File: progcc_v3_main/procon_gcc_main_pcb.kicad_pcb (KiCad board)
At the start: 4 copper layers, 110.9 x 59.7 mm, 108 parts, among them J1 Rumble, J2 Rumble, J3 To Button Board, J4 Conn_01x06_Female, J5 Conn_01x02_Pin, J9 USB_C_Receptacle, P1 Endpoint, Q1 Q_PMOS_GDS, Q2 Q_NMOS_GSD, Q3 Q_NMOS_GSD, Q4 BSS138, Q5 BSS138, Q6 BSS138, SW1 GL18_SW, SW2 GL18_SW, SW3 TS-1187A-B-A-B, T1 36-8730, T2 36-8730, T3 36-8730, T4 36-8730, U1 GH39F (Hall SOT23), U10 MCP3002, U11 ST_LSM6, U2 GH39F (Hall SOT23), U3 GH39F (Hall SOT23), U4 GH39F (Hall SOT23), U5 ST_LSM6, U6 RP2040, U7 LP3986-33B3F, U8 MCP3002, U9 W25Q128JVS, Y1 Crystal_GND3

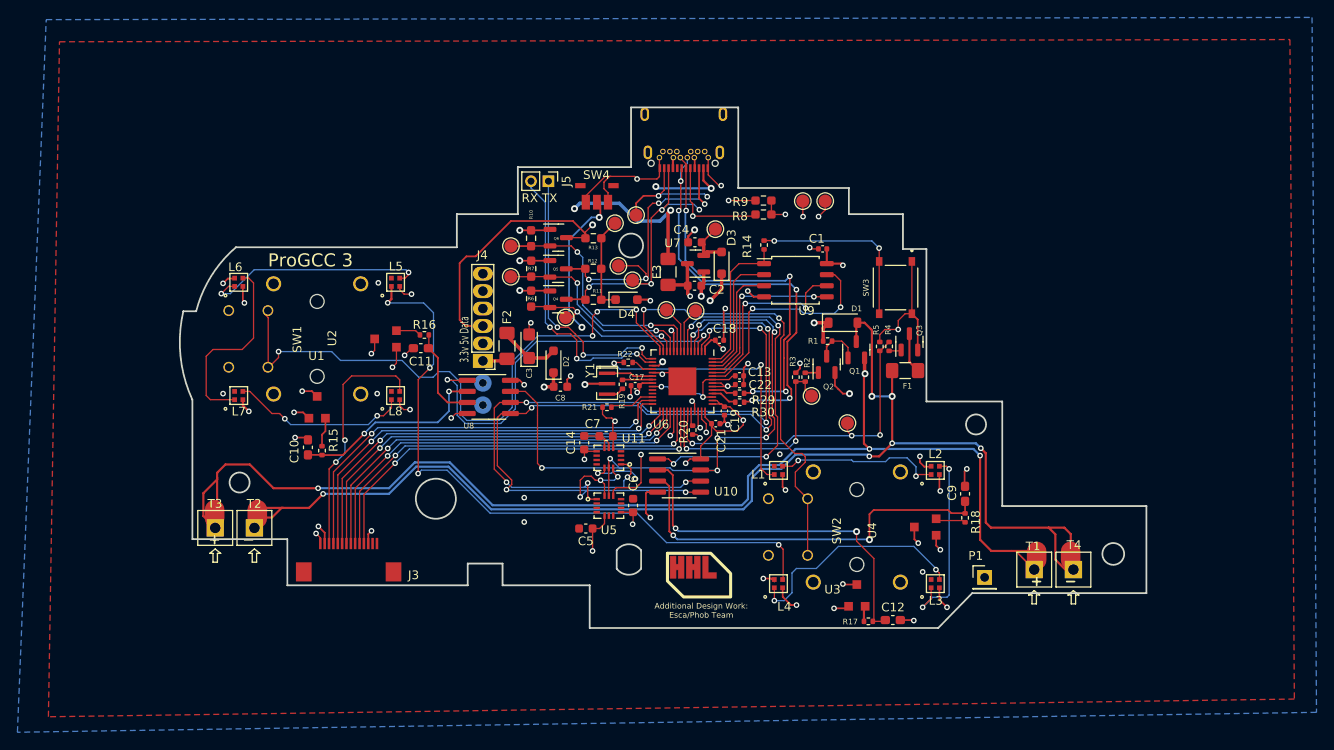
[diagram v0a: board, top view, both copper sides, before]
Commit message: remove D3
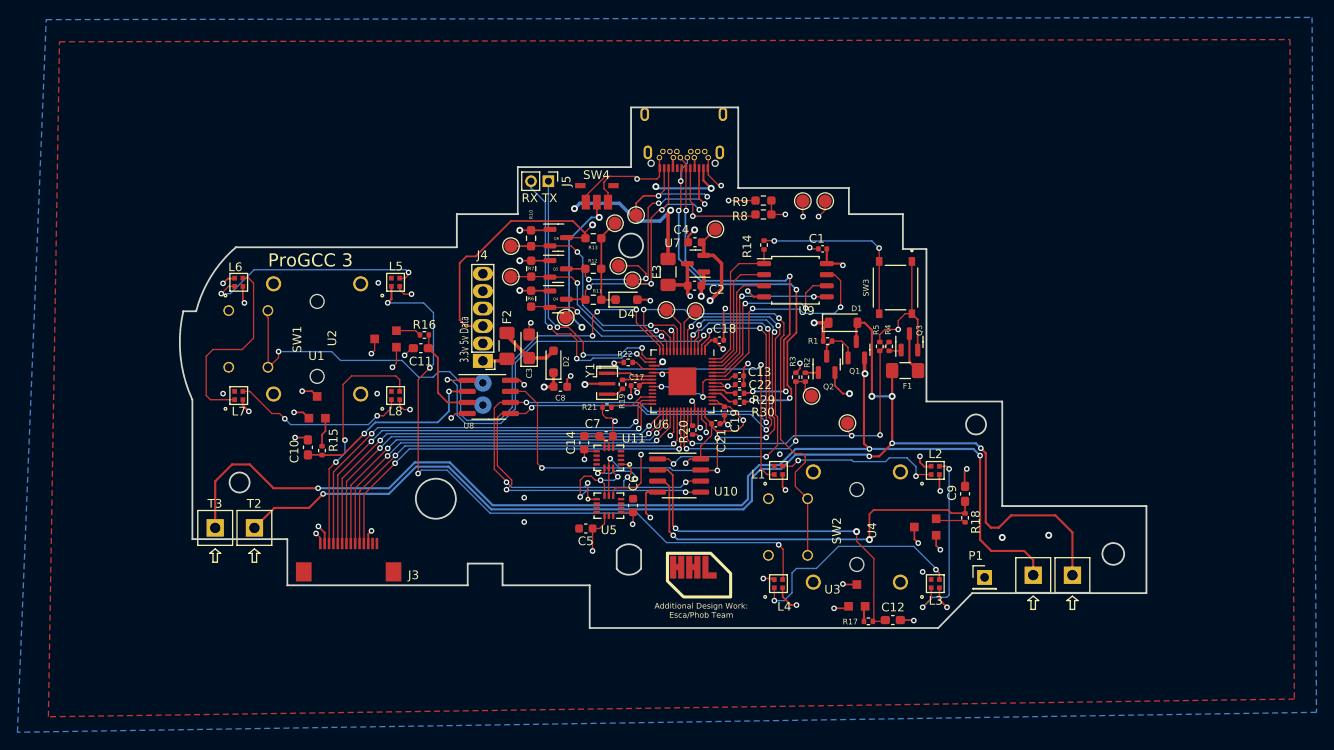
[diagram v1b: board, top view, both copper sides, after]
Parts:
- removed D3: CUS08F30, Diode_SMD:D_SOD-323_HandSoldering
- removed J1, J2: Rumble, progcc_v3:rumble_pins
- SW4: value ~ -> TS35CA
- moved T1 0.65 mm to (178.6, 145.5)
- moved T4 0.65 mm to (183.1, 145.5)
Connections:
- C4 pad 1: Net-(D3-A) -> +3V3
- TP13 pad 1: Net-(D3-A) -> +3V3
- U7 pad 2: Net-(D3-A) -> +3V3
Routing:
- net RUMBLE-: track 153.7 -> 141.1 mm
- net +5V: track 194.9 -> 183.6 mm
- net +3V3: track 103.5 -> 110.9 mm
- net Net-(D3-A): track 6.01 -> 0.00 mm
- net GND: vias 40 -> 42

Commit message: Update regulator
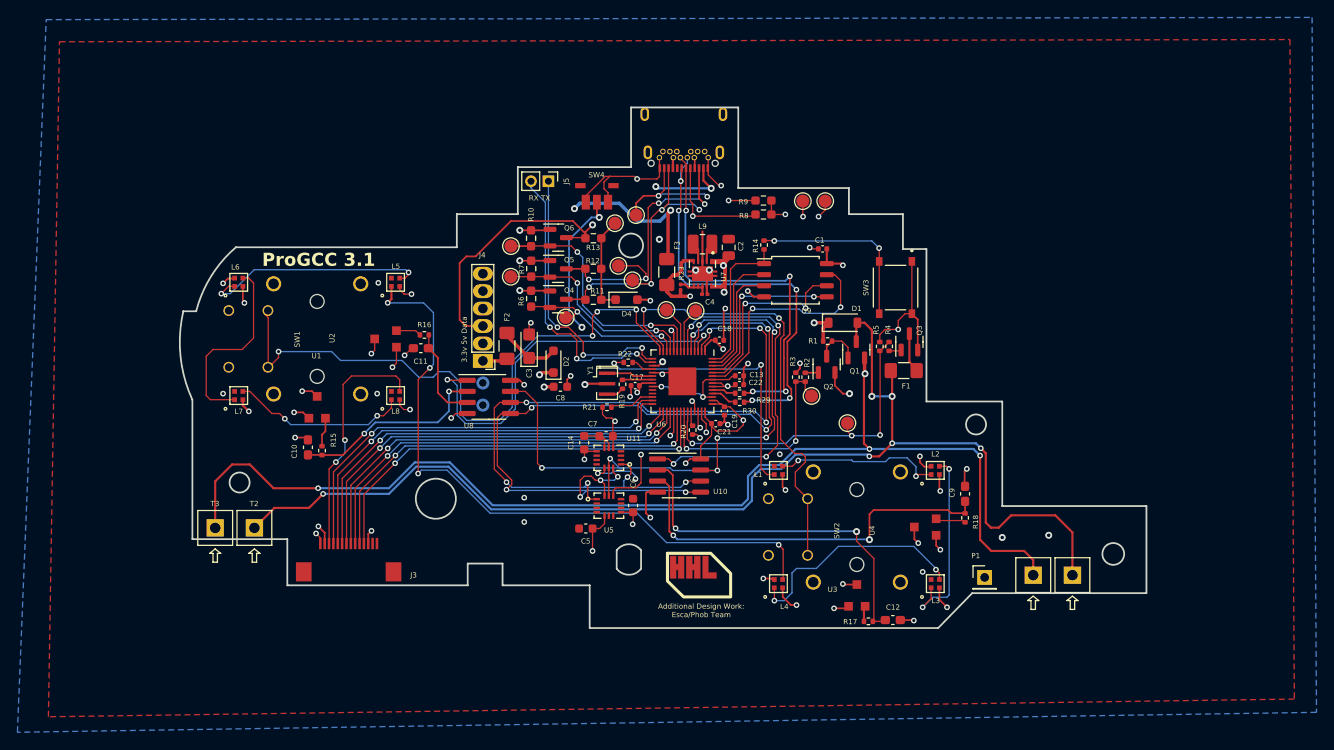
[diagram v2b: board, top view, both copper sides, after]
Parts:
- removed TP13: TestPoint, TestPoint:TestPoint_Pad_D1.5mm
- added L9: 1.3A 2.2uH ±20% 80mΩ, Inductor_SMD:L_1008_2520Metric, F.Cu at (140.6, 107.6)
- added R23: 100, Resistor_SMD:R_0201_0603Metric, F.Cu at (138.1, 112.5)
- C2: value 2.2uF -> 10uF; footprint Capacitor_SMD:C_0603_1608Metric -> Capacitor_SMD:C_0805_2012Metric
- C4: value 2.2uF -> 100n; footprint Capacitor_SMD:C_0603_1608Metric -> Capacitor_SMD:C_0201_0603Metric
- U7: value LP3986-33B3F -> TPS630001RCR; footprint Package_TO_SOT_SMD:SOT-23 -> hhl:VREG_V62_16624-01YE
- moved C4 6.07 mm to (140.9, 113.3)
- moved C2 5.90 mm to (143.6, 107.9), turned to 90 degrees
- moved U7 1.40 mm to (140.6, 111.0), turned to -90 degrees
- moved F1 0.15 mm to (163.7, 122.1)
- moved F3 0.15 mm to (136.5, 110.8)
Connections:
- C2 pad 1: +5V -> +3V3
- C4 pad 1: +3V3 -> GND
- C4 pad 2: GND -> Net-(U7-EN)
- D1 pad 1: +5V -> +VCC
- D2 pad 1: +3V3 -> +VCC
- F3 pad 2: +5V -> +VCC
- Q1 pad 2: +5V -> +VCC
- R1 pad 2: +5V -> +VCC
- T1 pad 1: +5V -> +VCC
- T3 pad 1: +5V -> +VCC
- TP9 pad 1: +5V -> +VCC
- U7 pad 1: GND -> +3V3
- U7 pad 2: +3V3 -> Net-(U7-L2)
- U7 pad 3: +5V -> GND
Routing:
- net +VCC: track 0.00 -> 210.7 mm, vias 0 -> 8
- net +5V: track 183.6 -> 0.00 mm, vias 7 -> 0
- net GND: track 106.7 -> 111.4 mm, vias 42 -> 43
- net Net-(U7-EN): track 0.00 -> 3.61 mm
- net +3V3: track 110.9 -> 108.3 mm, vias 33 -> 34
- net Net-(U7-L2): track 0.00 -> 2.23 mm
- net Net-(U7-L1): track 0.00 -> 2.22 mm
- net D-: track 84.0 -> 85.2 mm
- net D+: track 82.8 -> 83.8 mm
- net N_DATA: track 58.9 -> 58.4 mm
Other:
- board text added: "ProGCC 3.1"
- board text removed: "ProGCC 3"
